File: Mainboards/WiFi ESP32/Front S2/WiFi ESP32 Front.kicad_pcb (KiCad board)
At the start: 2 copper layers, 71.5 x 24 mm, 10 parts

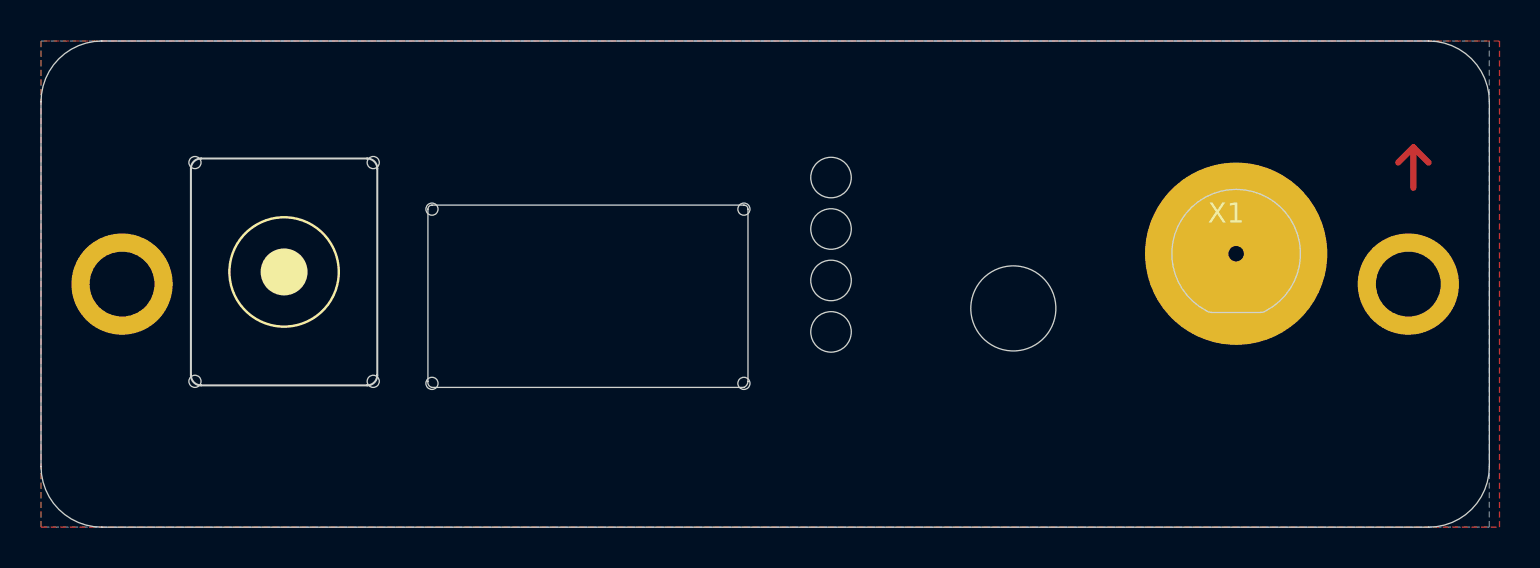
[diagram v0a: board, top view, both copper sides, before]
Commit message: Update TTY CL slave board
Add ESP32 S3 WiFi MasterBoard
Update libs
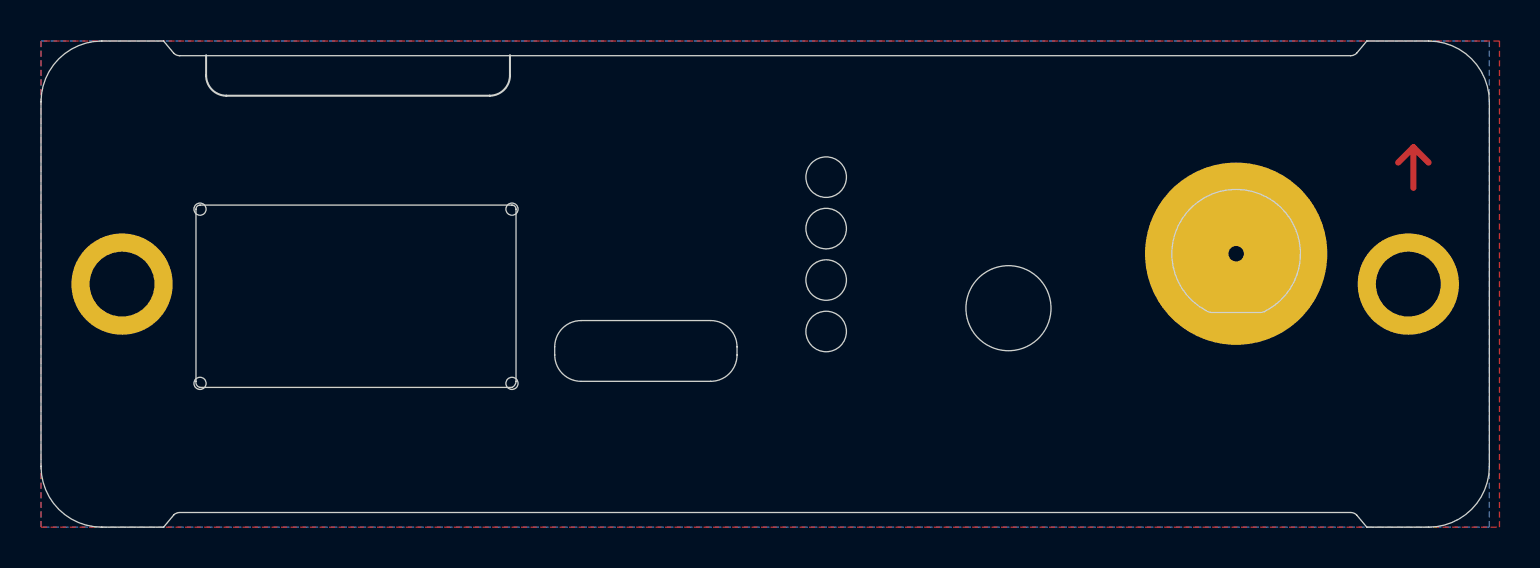
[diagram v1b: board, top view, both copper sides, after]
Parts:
- removed REF**: DC-front, AllSerial:DC-front
- moved E$2 11.4 mm to (134.0, 114.7)
- moved @HOLE2 0.24 mm to (157.2, 100.0)
- moved @HOLE4 0.24 mm to (157.2, 105.1)
- moved @HOLE1 0.24 mm to (157.2, 97.5)
- moved @HOLE3 0.24 mm to (157.2, 102.5)
- moved @HOLE0 0.24 mm to (166.2, 103.9)
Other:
- outline, holes or cut-outs redrawn
- board text added: "Ant"
- board text added: "USB-C"
- board text removed: "+"
- board text removed: "-"
- board text removed: "12 V in"

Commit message: Update AllSerial libraries
update projects
add slave project template
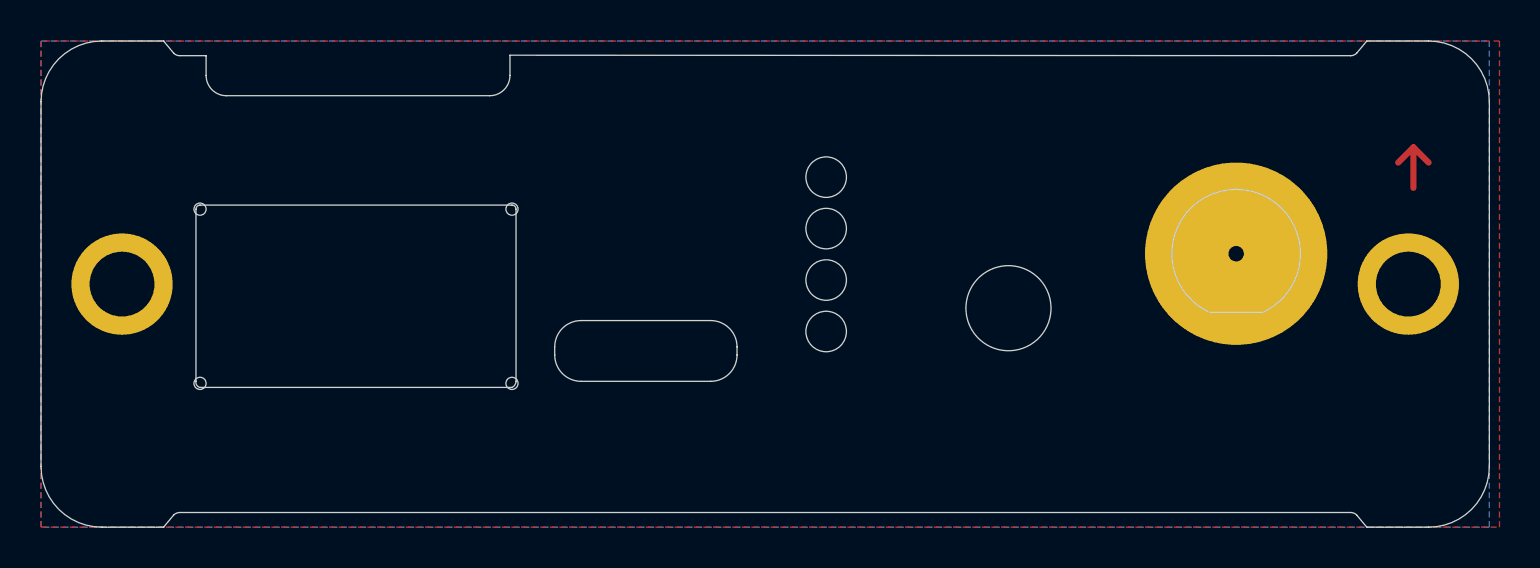
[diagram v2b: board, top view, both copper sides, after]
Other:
- outline, holes or cut-outs redrawn
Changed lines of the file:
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@@
 	(generator_version "8.0")
 	(general
-		(thickness 1.6)
+		(thickness 1.09)
 		(legacy_teardrops no)
 	)
@@
 	)
 	(setup
+		(stackup
+			(layer "F.SilkS"
+				(type "Top Silk Screen")
+			)
+			(layer "F.Paste"
+				(type "Top Solder Paste")
+			)
+			(layer "F.Mask"
+				(type "Top Solder Mask")
+				(thickness 0.01)
+			)
+			(layer "F.Cu"
+				(type "copper")
+				(thickness 0.035)
+			)
+			(layer "dielectric 1"
+				(type "core")
+				(thickness 1)
+				(material "FR4")
+				(epsilon_r 4.5)
+				(loss_tangent 0.02)
+			)
+			(layer "B.Cu"
+				(type "copper")
+				(thickness 0.035)
+			)
+			(layer "B.Mask"
+				(type "Bottom Solder Mask")
+				(thickness 0.01)
+			)
+			(layer "B.Paste"
+				(type "Bottom Solder Paste")
+			)
+			(layer "B.SilkS"
+				(type "Bottom Silk Screen")
+			)
+			(copper_finish "None")
+			(dielectric_constraints no)
+		)
 		(pad_to_mask_clearance 0)
 		(allow_soldermask_bridges_in_footprints no)
@@
 			(thermal_bridge_angle 90)
 		)
+		(model "${KICAD_USER_3D_DIR}/7587.stp"
+			(offset
+				(xyz 0 0 10)
+			)
+			(scale
+				(xyz 1 1 1)
+			)
+			(rotate
+				(xyz 0 -90 90)
+			)
+		)
 	)
 	(footprint ""
@@
 		(fp_arc
 			(start 29.25 -13.576875)
-			(mid 29.259131 -13.636641)
+			(mid 29.259139 -13.636635)
 			(end 29.285718 -13.690937)
 			(stroke
@@
 		(fp_arc
 			(start 29.285718 -10.269065)
-			(mid 29.259148 -10.323366)
+			(mid 29.259147 -10.323367)
 			(end 29.25 -10.383125)
 			(stroke
@@
 		(fp_arc
 			(start 30.098631 -12.980006)
-			(mid 30.180274 -12.96257)
+			(mid 30.180281 -12.962576)
 			(end 30.2477 -12.913337)
 			(stroke
@@
 		(fp_arc
 			(start 30.2477 -11.046665)
-			(mid 30.180281 -10.997415)
+			(mid 30.180274 -10.997429)
 			(end 30.098631 -10.980006)
 			(stroke
@@
 		(fp_arc
 			(start 30.2477 -11.046665)
-			(mid 30.53504 -11.179823)
+			(mid 30.53504 -11.179723)
 			(end 30.829168 -11.062355)
 			(stroke
@@
 		(fp_arc
 			(start 30.829168 -12.897646)
-			(mid 30.535037 -12.780118)
+			(mid 30.535038 -12.78003)
 			(end 30.247699 -12.913337)
 			(stroke
@@
 		(fp_arc
 			(start 30.829168 -12.897646)
-			(mid 30.991011 -13.03543)
+			(mid 30.991007 -13.035435)
 			(end 31.17314 -13.145006)
 			(stroke
@@
 		(fp_arc
 			(start 31.17314 -10.815006)
-			(mid 30.991006 -10.924569)
+			(mid 30.991008 -10.924571)
 			(end 30.829168 -11.062356)
 			(stroke
@@
 		(fp_arc
 			(start 31.404168 -9.000006)
-			(mid 30.208293 -9.40643)
+			(mid 30.208304 -9.406439)
 			(end 29.285718 -10.269065)
 			(stroke
@@
 		(fp_arc
 			(start 32.326868 -13.145006)
-			(mid 32.669238 -12.899238)
+			(mid 32.669227 -12.899227)
 			(end 32.915 -12.556865)
 			(stroke
@@
 		(fp_arc
 			(start 32.36654 -9.044037)
-			(mid 32.231689 -9.018925)
+			(mid 32.231688 -9.018931)
 			(end 32.095831 -9.000006)
 			(stroke
@@
 		(fp_arc
 			(start 32.49865 -9.139765)
-			(mid 32.442801 -9.077813)
+			(mid 32.442804 -9.077812)
 			(end 32.36654 -9.044037)
 			(stroke
@@
 		(fp_arc
 			(start 32.596368 -23.929275)
-			(mid 32.664857 -23.981462)
+			(mid 32.664857 -23.981453)
 			(end 32.74894 -24.000005)
 			(stroke
@@
 		(fp_arc
 			(start 32.74894 -24.000006)
-			(mid 34.870586 -23.121505)
+			(mid 34.870589 -23.121506)
 			(end 35.74944 -21.000004)
 			(stroke
@@
 		(fp_arc
 			(start 32.751109 -0.000006)
-			(mid 32.667352 -0.018662)
+			(mid 32.667367 -0.018676)
 			(end 32.59915 -0.070725)
 			(stroke
@@
 		(fp_arc
 			(start 32.75295 -9.126637)
-			(mid 32.759775 -9.178395)
+			(mid 32.759789 -9.178394)
 			(end 32.77974 -9.226637)
 			(stroke
@@
 		(fp_arc
 			(start 32.95295 -7.220006)
-			(mid 32.811563 -7.278603)
+			(mid 32.811528 -7.278597)
 			(end 32.75295 -7.420006)
 			(stroke
@@
 		(fp_arc
 			(start 34.9604 -9.000006)
-			(mid 35.0286 -8.988019)
+			(mid 35.028596 -8.988014)
 			(end 35.088618 -8.953487)
 			(stroke
@@
 		(fp_arc
 			(start 35.088581 -9.058575)
-			(mid 35.023693 -9.015234)
+			(mid 35.023694 -9.015223)
 			(end 34.947159 -9.000005)
 			(stroke
@@
 		(fp_arc
 			(start 35.689059 -6.946987)
-			(mid 35.739153 -6.873454)
+			(mid 35.73914 -6.873455)
 			(end 35.752381 -6.785475)
 			(stroke
@@
 		(fp_arc
 			(start 35.75 -9.802846)
-			(mid 35.734758 -9.726319)
+			(mid 35.73477 -9.726308)
 			(end 35.691418 -9.661424)
 			(stroke
@@
 		(fp_line
 			(start -28.9 -23.275736)
-			(end 28.9 -23.275736)
+			(end -27.6 -23.275736)
 			(stroke
 				(width 0.05)
@@
 		)
 		(fp_line
+			(start -27.6 -23.275736)
+			(end -27.6 -22.3)
+			(stroke
+				(width 0.05)
+				(type default)
+			)
+			(layer "Edge.Cuts")
+		)
+		(fp_line
+			(start -26.6 -21.3)
+			(end -13.6 -21.3)
+			(stroke
+				(width 0.05)
+				(type default)
+			)
+			(layer "Edge.Cuts")
+		)
+		(fp_line
+			(start -12.6 -23.3)
+			(end -12.6 -22.3)
+			(stroke
+				(width 0.05)
+				(type default)
+			)
+			(layer "Edge.Cuts")
+		)
+		(fp_line
+			(start 28.9 -23.275736)
+			(end -12.6 -23.3)
+			(stroke
+				(width 0.05)
+				(type default)
+			)
+			(layer "Edge.Cuts")
+		)
+		(fp_line
 			(start 29.7 -24)
 			(end 29.2 -23.4)
@@
 		)
 		(fp_arc
+			(start -26.6 -21.3)
+			(mid -27.307107 -21.592893)
+			(end -27.6 -22.3)
+			(stroke
+				(width 0.05)
+				(type default)
+			)
+			(layer "Edge.Cuts")
+		)
+		(fp_arc
+			(start -12.6 -22.3)
+			(mid -12.892893 -21.592893)
+			(end -13.6 -21.3)
+			(stroke
+				(width 0.05)
+				(type default)
+			)
+			(layer "Edge.Cuts")
+		)
+		(fp_arc
 			(start 28.9 -0.724264)
 			(mid 29.062359 -0.691969)
@@
 	)
 	(gr_line
-		(start 126.583 91.439)
-		(end 126.583 92.439)
-		(stroke
-			(width 0.1)
-			(type default)
-		)
-		(layer "Edge.Cuts")
-	)
-	(gr_line
 		(start 143.793 105.839)
 		(end 143.793 106.239)
@@
 	)
 	(gr_line
-		(start 141.583 91.439)
-		(end 141.583 92.439)
-		(stroke
-			(width 0.1)
-			(type default)
-		)
-		(layer "Edge.Cuts")
-	)
-	(gr_line
 		(start 145.093 107.539)
 		(end 151.493 107.539)
@@
 			(type default)
 		)
-		(layer "Edge.Cuts")
-	)
-	(gr_arc
-		(start 127.583 93.439)
-		(mid 126.875893 93.146107)
-		(end 126.583 92.439)
-		(stroke
-			(width 0.1)
-			(type default)
-		)
-		(layer "Edge.Cuts")
-	)
-	(gr_arc
-		(start 141.583 92.439)
-		(mid 141.290107 93.146107)
-		(end 140.583 93.439)
-		(stroke
-			(width 0.1)
-			(type default)
-		)
-		(layer "Edge.Cuts")
-	)
-	(gr_line
-		(start 127.583 93.439)
-		(end 140.583 93.439)
-		(stroke
-			(width 0.1)
-			(type default)
-		)

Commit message: Migrate to KiCad 9
Add eBus board
Add various libraries
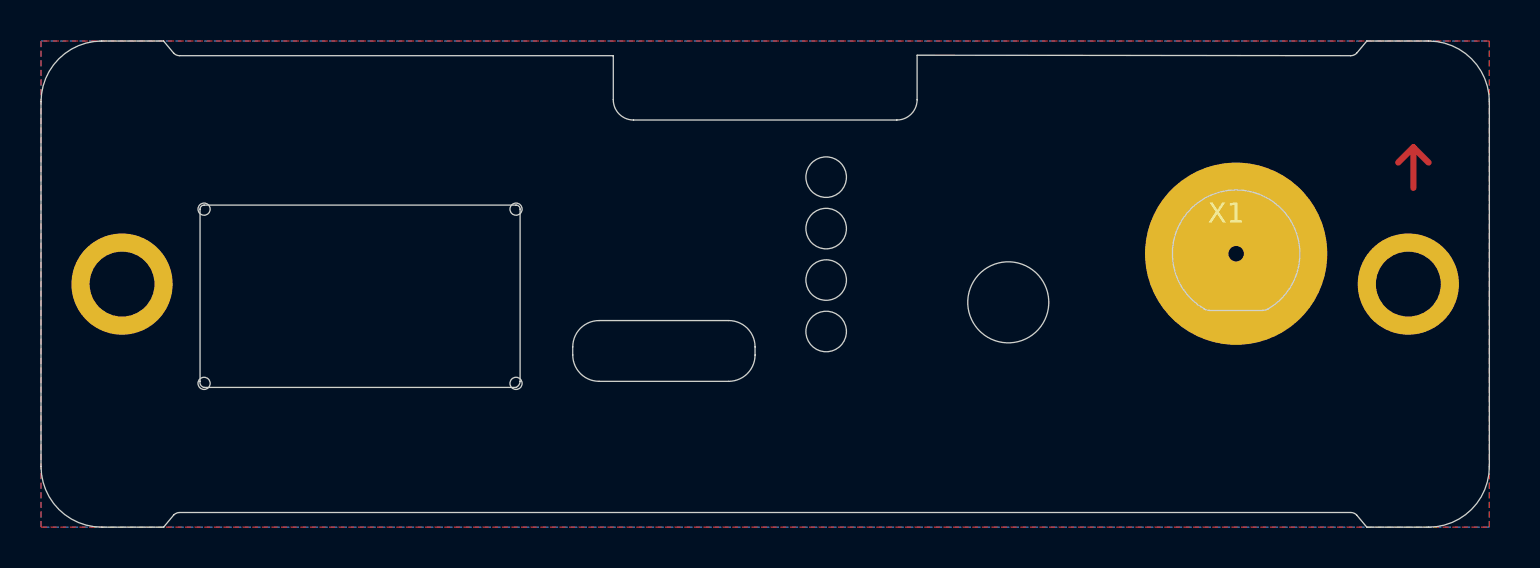
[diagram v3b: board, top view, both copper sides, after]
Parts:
- moved @HOLE0 0.29 mm to (166.2, 103.6)
- moved E$2 0.20 mm to (134.2, 114.7)
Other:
- outline, holes or cut-outs redrawn
- board text added: "AllSerial WiFi Master 30/24"
- board text removed: "AllSerial WiFi Master 27/24"

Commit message: improve AllSerial library
add assets for README
update README
cleanup
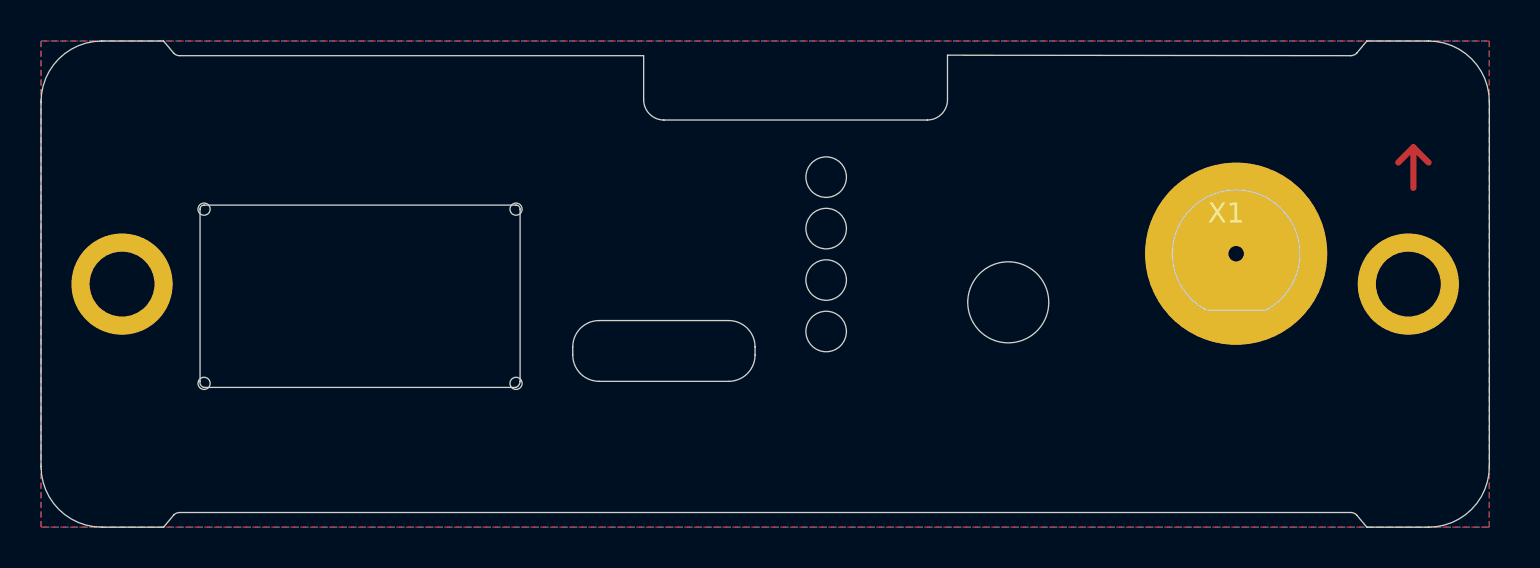
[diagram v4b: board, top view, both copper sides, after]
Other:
- outline, holes or cut-outs redrawn
- board text added: "AllSerial WiFi Master 26/25"
- board text removed: "AllSerial WiFi Master 30/24"
